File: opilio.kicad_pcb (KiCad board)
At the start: 4 copper layers, 75 x 46 mm, 113 parts, among them J1 SATA_Power_Connector, J2 USB_C_Receptacle_USB2.0, J3 Conn_01x04_Male, J6 Conn_01x06_Male, Q1 CJ3134KW, Q2 AO3401A, Q3 CJ3134KW, Q4 AO3401A, SW1 Reset, SW2 Boot, U1 EUP3458, U2 STM32F103C8T6, U3 USBLC6-2SC6, Y1 TAXM8M4RFDCET2T, Y2 YST310S 32.768KHz

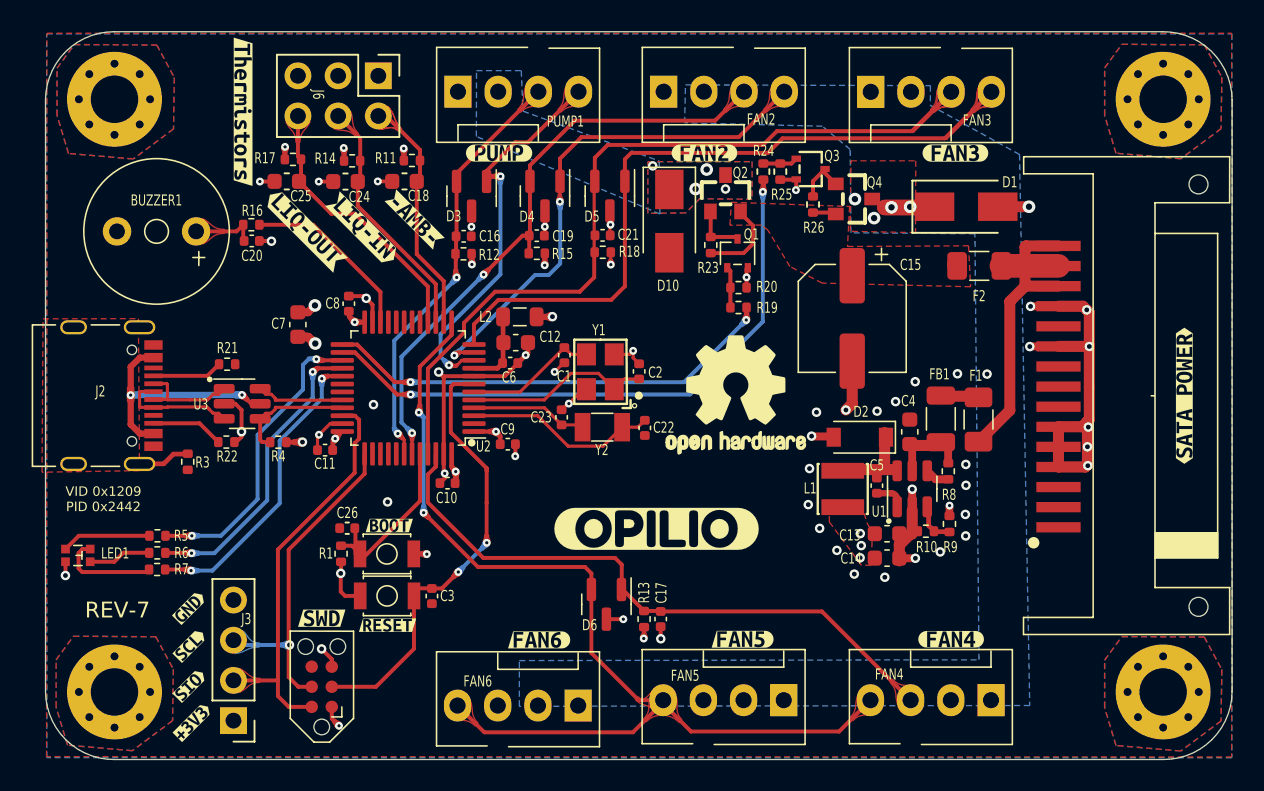
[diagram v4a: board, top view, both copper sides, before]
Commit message: split schema, re-route, horizontal fan connectors
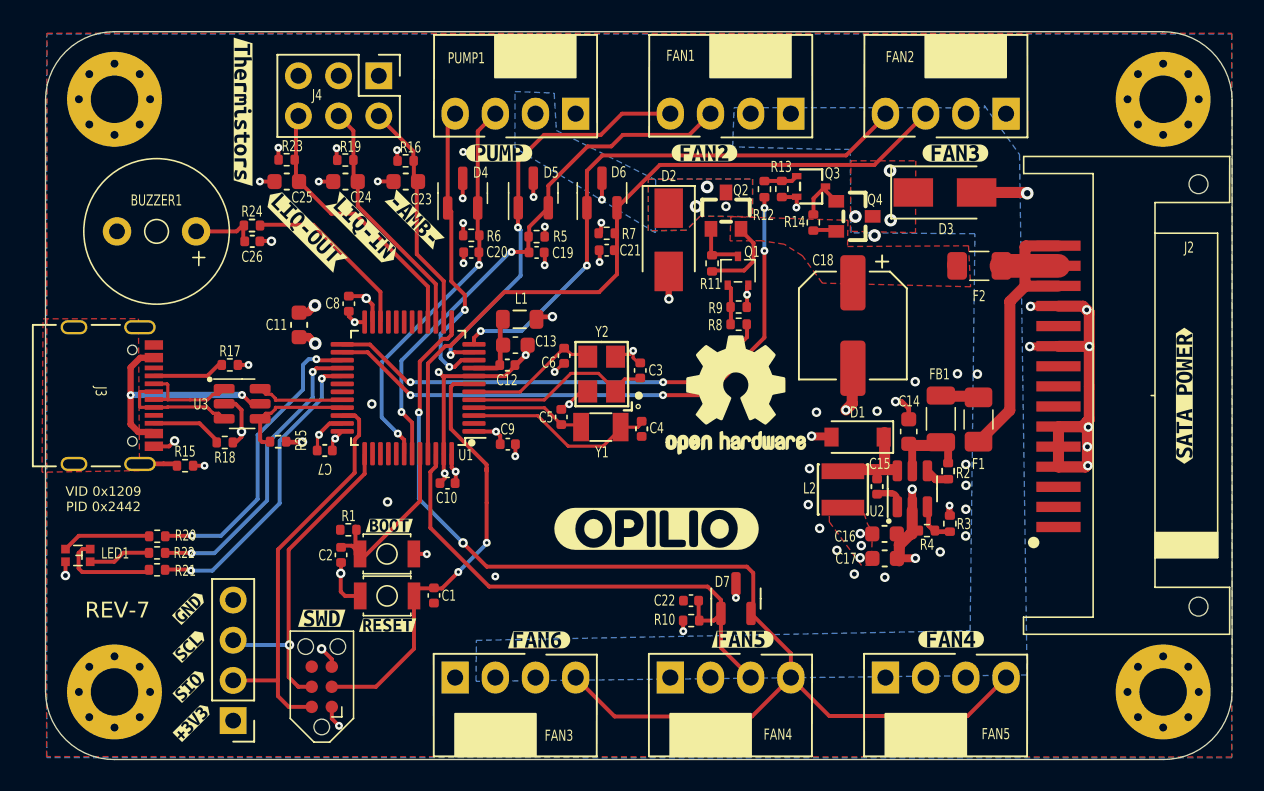
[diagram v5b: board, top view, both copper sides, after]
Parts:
- removed D10: B230A, Diode_SMD:D_SMA
- removed FAN6: Fan_4pin, Custom:FanPinHeader_1x04_P2.54mm_Vertical_no_hole
- removed J6: Conn_01x06_Male, Connector_PinHeader_2.54mm:PinHeader_2x03_P2.54mm_Vertical
- removed R26: 10K, Resistor_SMD:R_0402_1005Metric
- added D7: SP0502BAHT, Package_TO_SOT_SMD:SOT-23, F.Cu at (148.7, 132.8)
- added FAN1: Fan_4pin, Custom:FanPinHeader_1x04_P2.54mm_Horizontal_no_hole, F.Cu at (148.4, 102.2)
- added J4: Conn_01x06_Male, Connector_PinHeader_2.54mm:PinHeader_2x03_P2.54mm_Vertical, F.Cu at (126.1, 99.8)
- added R2: 1K5, Resistor_SMD:R_0402_1005Metric, F.Cu at (162.1, 124.8)
- C1, C2: value 18pF -> 100nF
- C11: value 100nF -> 10uF; footprint Capacitor_SMD:C_0402_1005Metric -> Capacitor_SMD:C_0603_1608Metric
- C12: value 10uF -> 10nF; footprint Capacitor_SMD:C_0603_1608Metric -> Capacitor_SMD:C_0402_1005Metric
- C15: value 220uF -> 10nF; footprint Capacitor_SMD:CP_Elec_6.3x7.7 -> Capacitor_SMD:C_0402_1005Metric
- C16, C17: value 10nF -> 10uF; footprint Capacitor_SMD:C_0402_1005Metric -> Capacitor_SMD:C_0603_1608Metric
- C18: value 10uF -> 220uF; footprint Capacitor_SMD:C_0603_1608Metric -> Capacitor_SMD:CP_Elec_6.3x7.7
- C20: value 100nF -> 10nF
- C22: value 18pF -> 10nF
- C23: value 18pF -> 10uF; footprint Capacitor_SMD:C_0402_1005Metric -> Capacitor_SMD:C_0603_1608Metric
- C3: value 100nF -> 18pF
- C4: value 10uF -> 18pF; footprint Capacitor_SMD:C_0603_1608Metric -> Capacitor_SMD:C_0402_1005Metric
- C5, C6: value 10nF -> 18pF
- C7: value 10uF -> 100nF; footprint Capacitor_SMD:C_0603_1608Metric -> Capacitor_SMD:C_0402_1005Metric
- D1: value B230A -> B5819W; footprint Diode_SMD:D_SMA -> Diode_SMD:D_SOD-123
- D2: value B5819W -> B230A; footprint Diode_SMD:D_SOD-123 -> Diode_SMD:D_SMA
- D3: value SP0502BAHT -> B230A; footprint Package_TO_SOT_SMD:SOT-23 -> Diode_SMD:D_SMA
- FAN2, FAN3, FAN4, FAN5, PUMP1: footprint Custom:FanPinHeader_1x04_P2.54mm_Vertical_no_hole -> Custom:FanPinHeader_1x04_P2.54mm_Horizontal_no_hole
- J1: value SATA_Power_Connector -> Conn_01x04_Male; footprint Custom:Sata_Power_Connector_SMD -> Connector_PinHeader_2.54mm:PinHeader_1x04_P2.54mm_Vertical
- J2: value USB_C_Receptacle_USB2.0 -> SATA_Power_Connector; footprint Custom:USB_C_Receptacle_Palconn_UTC16-G_Streached_pads -> Custom:Sata_Power_Connector_SMD
- J3: value Conn_01x04_Male -> USB_C_Receptacle_USB2.0; footprint Connector_PinHeader_2.54mm:PinHeader_1x04_P2.54mm_Vertical -> Custom:USB_C_Receptacle_Palconn_UTC16-G_Streached_pads
- L1: value SMNR3010-4R7MT -> 39nH; footprint easyeda2kicad:IND-SMD_L3.0-W3.0_SMNR3010 -> Inductor_SMD:L_0805_2012Metric
- L2: value 39nH -> SMNR3010-4R7MT; footprint Inductor_SMD:L_0805_2012Metric -> easyeda2kicad:IND-SMD_L3.0-W3.0_SMNR3010
- R10: value 24K -> 1K5
- R12, R8: value 1K5 -> 0R
- R13: value 1K5 -> 10K
- R15: value 1K5 -> 75K
- R16: value 100R -> 10K
- R17: value 10K -> 5K11
- R18: value 1K5 -> 5K11
- R19: value 0R -> 10K
- R20, R25: value 10K -> 1K5
- R21, R22: value 5K11 -> 1K5
- R24: value 0R -> 100R
- R4: value 1K5 -> 24K
- R9: value 75K -> 10K
- U1: value EUP3458 -> STM32F103C8T6; footprint Package_TO_SOT_SMD:SOT-23-6 -> Package_QFP:LQFP-48_7x7mm_P0.5mm
- U2: value STM32F103C8T6 -> EUP3458; footprint Package_QFP:LQFP-48_7x7mm_P0.5mm -> Package_TO_SOT_SMD:SOT-23-6
- Y1: value TAXM8M4RFDCET2T -> YST310S 32.768KHz; footprint easyeda2kicad:OSC-SMD_4P-L3.2-W2.5-BL -> Crystal:Crystal_SMD_3215-2Pin_3.2x1.5mm
- Y2: value YST310S 32.768KHz -> TAXM8M4RFDCET2T; footprint Crystal:Crystal_SMD_3215-2Pin_3.2x1.5mm -> easyeda2kicad:OSC-SMD_4P-L3.2-W2.5-BL
- moved J2 58.6 mm to (167.7, 120.0), turned to 90 degrees
- moved J1 54.8 mm to (116.9, 140.6), turned to 180 degrees
- moved R3 48.3 mm to (162.2, 128.1), turned to -90 degrees
- moved FAN3 43.5 mm to (134.8, 137.8)
- moved R4 41.4 mm to (160.8, 128.6)
- moved R20 40.0 mm to (112.1, 128.9)
- moved R25 36.0 mm to (119.8, 122.9), turned to 180 degrees
- moved R7 35.5 mm to (140.6, 109.8), turned to 0 degrees
- moved C16 32.6 mm to (158.1, 128.8), turned to 0 degrees
- moved U2 32.5 mm to (159.9, 125.9), turned to 90 degrees
- moved R24 32.5 mm to (118.1, 109.3), turned to 180 degrees
- moved U1 32.5 mm to (128.0, 119.5), turned to 180 degrees
- moved R5 30.5 mm to (136.1, 110.0)
- moved D3 29.9 mm to (161.9, 107.2), turned to 0 degrees
- moved C18 29.8 mm to (156.1, 115.6), turned to -90 degrees
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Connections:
- C1 pad 1: OSCOUT -> NRST
- C13 pad 1: +3.3V -> VDDA
- C14 pad 1: +3.3V -> Net-(C14-Pad1)
- C15 pad 1: +12VF(F) -> Net-(C15-Pad1)
- C15 pad 2: GND -> Net-(C15-Pad2)
- C16 pad 1: GND -> +3.3V
- C16 pad 2: PWM_READ1 -> GND
- C17 pad 1: GND -> +3.3V
- C17 pad 2: PWM_READ4 -> GND
- C18 pad 1: AMBIENT_T -> +12VF(F)
- C2 pad 1: GND -> BOOT0
- C2 pad 2: OSCIN -> GND
- C20 pad 1: Net-(BUZZER1-Pad1) -> GND
- C20 pad 2: GND -> PWM_READ1
- C22 pad 1: CIN -> GND
- C22 pad 2: GND -> PWM_READ4
- C23 pad 1: COUT -> AMBIENT_T
- C26 pad 1: BOOT0 -> Net-(BUZZER1-Pad1)
- C3 pad 1: NRST -> GND
- C3 pad 2: GND -> OSCIN
- C4 pad 1: Net-(C4-Pad1) -> CIN
- C5 pad 1: Net-(C5-Pad1) -> COUT
- C5 pad 2: Net-(C5-Pad2) -> GND
- C6 pad 1: VDDA -> OSCOUT
- D1 pad 1: 12vC -> Net-(C15-Pad1)
- D2 pad 1: Net-(C5-Pad1) -> 12vP
- D3 pad 1: PWM_OUT1 -> 12vC
- D3 pad 2: PWM_READ1 -> GND
- D4 pad 1: PWM_OUT2 -> PWM_OUT1
- D4 pad 2: PWM_READ2 -> PWM_READ1
- D5 pad 1: PWM_OUT3 -> PWM_OUT2
- D5 pad 2: PWM_READ3 -> PWM_READ2
- D6 pad 1: PWM_READ4 -> PWM_OUT3
- D6 pad 2: PWM_OUT4 -> PWM_READ3
- FAN2 pad 3: PWM_READ2 -> PWM_READ3
- FAN2 pad 4: PWM_OUT2 -> PWM_OUT3
- FAN3 pad 3: PWM_READ3 -> unconnected-(FAN3-Pad3)
- FAN3 pad 4: PWM_OUT3 -> PWM_OUT4
- FB1 pad 1: Net-(C4-Pad1) -> Net-(C14-Pad1)
- J1 pad 1: unconnected-(J1-Pad1) -> +3.3V
- J1 pad 2: unconnected-(J1-Pad2) -> SWIO
- J1 pad 3: unconnected-(J1-Pad3) -> SWCLK
- L1 pad 1: Net-(C5-Pad1) -> +3.3V
- L1 pad 2: +3.3V -> VDDA
- L2 pad 1: +3.3V -> Net-(C15-Pad1)
- L2 pad 2: VDDA -> +3.3V
- R10 pad 1: BUCK_FB -> +3.3V
- R10 pad 2: GND -> PWM_READ4
- R11 pad 1: AMBIENT_T -> +12VF(F)
- R11 pad 2: +3.3V -> Net-(Q1-Pad3)
- R12 pad 1: +3.3V -> FAN_EN
- R12 pad 2: PWM_READ1 -> Net-(Q3-Pad1)
- R13 pad 1: +3.3V -> GND
- R13 pad 2: PWM_READ4 -> Net-(Q3-Pad1)
- R14 pad 1: WATER_IN_T -> +12VF(F)
- R14 pad 2: +3.3V -> Net-(Q3-Pad3)
- R15 pad 1: +3.3V -> GND
- R15 pad 2: PWM_READ2 -> Net-(J3-PadS1)
- R16 pad 1: BUZZER -> AMBIENT_T
- R16 pad 2: Net-(BUZZER1-Pad1) -> +3.3V
- R17 pad 1: WATER_OUT_T -> GND
- R17 pad 2: +3.3V -> Net-(J3-PadA5)
- R18 pad 1: +3.3V -> GND
- R18 pad 2: PWM_READ3 -> Net-(J3-PadB5)
- R19 pad 1: PUMP_EN -> WATER_IN_T
- R19 pad 2: Net-(Q1-Pad1) -> +3.3V
- R20 pad 1: GND -> RED_LED
- R20 pad 2: Net-(Q1-Pad1) -> Net-(LED1-Pad1)
- R21 pad 1: GND -> GREEN_LED
- R21 pad 2: Net-(J2-PadA5) -> Net-(LED1-Pad2)
- R22 pad 1: GND -> BLUE_LED
- R22 pad 2: Net-(J2-PadB5) -> Net-(LED1-Pad4)
- R23 pad 1: +12VF(F) -> WATER_OUT_T
- R23 pad 2: Net-(Q1-Pad3) -> +3.3V
- R24 pad 1: FAN_EN -> BUZZER
- R24 pad 2: Net-(Q3-Pad1) -> Net-(BUZZER1-Pad1)
- R25 pad 1: GND -> +3.3V
- R25 pad 2: Net-(Q3-Pad1) -> USB_D+
- R3 pad 1: GND -> +3.3V
- R3 pad 2: Net-(J2-PadS1) -> BUCK_FB
- R4 pad 1: +3.3V -> BUCK_FB
- R4 pad 2: USB_D+ -> GND
- R5 pad 1: RED_LED -> +3.3V
- R5 pad 2: Net-(LED1-Pad1) -> PWM_READ2
- R6 pad 1: BLUE_LED -> +3.3V
- R6 pad 2: Net-(LED1-Pad4) -> PWM_READ1
- R7 pad 1: GREEN_LED -> +3.3V
- R7 pad 2: Net-(LED1-Pad2) -> PWM_READ3
- R8 pad 1: Net-(C4-Pad1) -> PUMP_EN
- R8 pad 2: Net-(R8-Pad2) -> Net-(Q1-Pad1)
- R9 pad 1: +3.3V -> GND
- R9 pad 2: BUCK_FB -> Net-(Q1-Pad1)
- U1 pad 1: Net-(C5-Pad2) -> +3.3V
- U1 pad 2: GND -> unconnected-(U1-Pad2)
- U1 pad 3: BUCK_FB -> CIN
- U1 pad 4: Net-(R8-Pad2) -> COUT
- U1 pad 5: Net-(C4-Pad1) -> OSCIN
- U1 pad 6: Net-(C5-Pad1) -> OSCOUT
- U2 pad 1: +3.3V -> Net-(C15-Pad2)
- U2 pad 2: unconnected-(U2-Pad2) -> GND
- U2 pad 3: CIN -> BUCK_FB
- U2 pad 4: COUT -> Net-(R2-Pad2)
- U2 pad 5: OSCIN -> Net-(C14-Pad1)
- U2 pad 6: OSCOUT -> Net-(C15-Pad1)
- Y1 pad 1: OSCIN -> CIN
- Y1 pad 2: GND -> COUT
- Y2 pad 1: CIN -> OSCIN
- Y2 pad 2: COUT -> GND
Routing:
- net PWM_OUT3: track 59.3 -> 35.7 mm, vias 0 -> 2
- net PWM_READ3: track 62.6 -> 46.2 mm
- net PWM_OUT4: track 65.2 -> 74.0 mm
- net GND: track 85.1 -> 93.6 mm, vias 56 -> 64
- net PWM_READ2: track 42.0 -> 33.8 mm
- net PWM_OUT1: track 25.9 -> 18.6 mm
- net Net-(C5-Pad1): track 6.75 -> 0.00 mm
- net Net-(C15-Pad1): track 0.00 -> 6.75 mm
- net PWM_OUT2: track 33.0 -> 26.6 mm
- net PWM_READ4: track 39.8 -> 33.5 mm
- net Net-(C4-Pad1): track 5.07 -> 0.00 mm
- net Net-(C14-Pad1): track 0.00 -> 5.07 mm
- net Net-(J3-PadB5): track 0.00 -> 4.59 mm
- net Net-(J2-PadB5): track 4.59 -> 0.00 mm
- net Net-(J3-PadA5): track 0.00 -> 4.45 mm
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- added copper zone on F.Cu, net Net-(J3-PadS1)
- removed copper zone on F.Cu, net Net-(J2-PadS1)

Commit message: rev-7 ready
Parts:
- removed kibuzzard-63630176: G***, kibuzzard-63630176
- removed kibuzzard-6364685F: G***, kibuzzard-6364685F
- removed kibuzzard-6368E60E: G***, kibuzzard-6368E60E
- removed kibuzzard-6368E619: G***, kibuzzard-6368E619
- removed kibuzzard-6368E624: G***, kibuzzard-6368E624
- added REF**: Fiducial_0.5mm_Mask1mm, Fiducial:Fiducial_0.5mm_Mask1mm, F.Cu at (169.6, 102.0)
- added REF**: Fiducial_0.5mm_Mask1mm, Fiducial:Fiducial_0.5mm_Mask1mm, F.Cu at (169.6, 138.0)
- added REF**: Fiducial_0.5mm_Mask1mm, Fiducial:Fiducial_0.5mm_Mask1mm, F.Cu at (142.6, 120.0)
- added kibuzzard-636BA6E5: G***, kibuzzard-636BA6E5, F.Cu at (119.9, 141.6)
- added kibuzzard-636BA708: G***, kibuzzard-636BA708, F.Cu at (129.6, 128.5)
- added kibuzzard-636BA711: G***, kibuzzard-636BA711, F.Cu at (129.9, 133.0)
- added kibuzzard-636C2D8A: G***, kibuzzard-636C2D8A, F.Cu at (148.2, 135.4)
- added kibuzzard-636C2D92: G***, kibuzzard-636C2D92, F.Cu at (162.3, 135.4)
- L1: footprint Inductor_SMD:L_0805_2012Metric -> Inductor_SMD:L_0603_1608Metric
- SW1: value Reset -> TS-1077S-01726; footprint easyeda2kicad:SW-SMD_L3.0-W2.5-P3.40-LS4.0-L -> easyeda2kicad:KEY-SMD_4P-L3.1-W3.1-P2.00_TS-1077S-01726
- SW2: value Boot -> TS-1077S-01726; footprint easyeda2kicad:SW-SMD_L3.0-W2.5-P3.40-LS4.0-L -> easyeda2kicad:KEY-SMD_4P-L3.1-W3.1-P2.00_TS-1077S-01726
- moved C1 6.28 mm to (123.4, 133.0), turned to 90 degrees
- moved C2 5.58 mm to (127.2, 125.7), turned to 180 degrees
- moved kibuzzard-6363013C 1.80 mm to (148.5, 104.6)
- moved kibuzzard-63646865 1.56 mm to (134.7, 135.4)
- moved SW2 1.55 mm to (126.3, 128.5)
- moved kibuzzard-636300D1 1.46 mm to (135.2, 104.6)
- moved R1 0.96 mm to (123.3, 128.6), turned to -90 degrees
- moved SW1 0.44 mm to (126.3, 132.9)
- moved L1 0.29 mm to (134.8, 115.3)
- moved R24 0.19 mm to (118.2, 109.1)
- moved C26 0.19 mm to (118.2, 110.1)
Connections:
- SW1 pad 1: GND -> NRST
- SW2 pad 1: BOOT0 -> +3.3V
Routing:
- net NRST: track 29.7 -> 34.8 mm
- net GND: track 93.6 -> 98.1 mm, vias 64 -> 65
- net +3.3V: track 18.7 -> 22.1 mm
- net BOOT0: track 11.6 -> 10.1 mm
- net 12vP: vias 3 -> 4
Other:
- board text added: "*"
- board text added: "0.25A"
- board text added: "2A"

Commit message: fix led polarity
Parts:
- removed REF** (x3): Fiducial_0.5mm_Mask1mm, Fiducial:Fiducial_0.5mm_Mask1mm
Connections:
- LED1 pad 3: GND -> +3.3V
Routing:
- net GND: track 98.1 -> 97.2 mm, vias 65 -> 64
- net +3.3V: track 22.1 -> 23.0 mm, vias 20 -> 21
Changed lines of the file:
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@@
     )
   )
-  (footprint "Fiducial:Fiducial_0.5mm_Mask1mm" (layer "F.Cu")
-    (at 169.58 102.02)
-    (descr "Circular Fiducial, 0.5mm bare copper, 1mm soldermask opening (Level C)")
-    (tags "fiducial")
-    (attr smd)
-    (fp_text reference "REF**" (at 2.78 0.91) (layer "F.SilkS") hide
-      (effects (font (size 1 1) (thickness 0.15)))
-    )
-    (fp_text value "Fiducial_0.5mm_Mask1mm" (at 0 1.5) (layer "F.Fab")
-      (effects (font (size 1 1) (thickness 0.15)))
-    )
-    (fp_text user "${REFERENCE}" (at 0 0) (layer "F.Fab")
-      (effects (font (size 0.2 0.2) (thickness 0.04)))
-    )
-    (fp_circle (center 0 0) (end 0.6 0.02) (layer "F.CrtYd") (width 0.05) (fill none))
-    (fp_circle (center 0 0) (end 0.5 0) (layer "F.Fab") (width 0.1) (fill none))
-    (pad "" smd circle (at 0 0) (size 0.5 0.5) (layers "F.Cu" "F.Mask")
-      (solder_mask_margin 0.25) (clearance 0.25))
-  )
   (footprint "Resistor_SMD:R_0402_1005Metric" locked (layer "F.Cu")
     (at 160.79 128.55 180)
@@
       (net 40 "Net-(LED1-Pad2)") (pinfunction "2") (pintype "unspecified"))
     (pad "3" smd rect locked (at 0.78 -0.4) (size 0.55 0.55) (layers "F.Cu" "F.Paste" "F.Mask")
-      (net 3 "GND") (pinfunction "3") (pintype "unspecified"))
+      (net 29 "+3.3V") (pinfunction "3") (pintype "unspecified"))
     (pad "4" smd rect locked (at -0.78 -0.4) (size 0.55 0.55) (layers "F.Cu" "F.Paste" "F.Mask")
       (net 41 "Net-(LED1-Pad4)") (pinfunction "4") (pintype "unspecified"))
@@
     )
   )
-  (footprint "Fiducial:Fiducial_0.5mm_Mask1mm" (layer "F.Cu")
-    (at 169.58 138.02)
-    (descr "Circular Fiducial, 0.5mm bare copper, 1mm soldermask opening (Level C)")
-    (tags "fiducial")
-    (attr smd)
-    (fp_text reference "REF**" (at 2.78 0.91) (layer "F.SilkS") hide
-      (effects (font (size 1 1) (thickness 0.15)))
-    )
-    (fp_text value "Fiducial_0.5mm_Mask1mm" (at 0 1.5) (layer "F.Fab")
-      (effects (font (size 1 1) (thickness 0.15)))
-    )
-    (fp_text user "${REFERENCE}" (at 0 0) (layer "F.Fab")
-      (effects (font (size 0.2 0.2) (thickness 0.04)))
-    )
-    (fp_circle (center 0 0) (end 0.6 0.02) (layer "F.CrtYd") (width 0.05) (fill none))
-    (fp_circle (center 0 0) (end 0.5 0) (layer "F.Fab") (width 0.1) (fill none))
-    (pad "" smd circle (at 0 0) (size 0.5 0.5) (layers "F.Cu" "F.Mask")
-      (solder_mask_margin 0.25) (clearance 0.25))
-  )
   (footprint "kibuzzard-63646865" (layer "F.Cu")
     (at 134.72 135.4)
@@
       ) (layer "F.SilkS") (width 0) (fill solid))
   )
-  (footprint "Fiducial:Fiducial_0.5mm_Mask1mm" (layer "F.Cu")
-    (at 142.58 120.02)
-    (descr "Circular Fiducial, 0.5mm bare copper, 1mm soldermask opening (Level C)")
-    (tags "fiducial")
-    (attr smd)
-    (fp_text reference "REF**" (at 2.78 0.91) (layer "F.SilkS") hide
-      (effects (font (size 1 1) (thickness 0.15)))
-    )
-    (fp_text value "Fiducial_0.5mm_Mask1mm" (at 0 1.5) (layer "F.Fab")
-      (effects (font (size 1 1) (thickness 0.15)))
-    )
-    (fp_text user "${REFERENCE}" (at 0 0) (layer "F.Fab")
-      (effects (font (size 0.2 0.2) (thickness 0.04)))
-    )
-    (fp_circle (center 0 0) (end 0.6 0.02) (layer "F.CrtYd") (width 0.05) (fill none))
-    (fp_circle (center 0 0) (end 0.5 0) (layer "F.Fab") (width 0.1) (fill none))
-    (pad "" smd circle (at 0 0) (size 0.5 0.5) (layers "F.Cu" "F.Mask")
-      (solder_mask_margin 0.25) (clearance 0.25))
-  )
   (footprint "Resistor_SMD:R_0402_1005Metric" (layer "F.Cu")
     (at 147.21 111.66 90)
@@
   (segment (start 170.81 124.53) (end 170.935 124.405) (width 0.7) (layer "F.Cu") (net 3))
   (segment (start 136.64 110.95) (end 136.64 111.73) (width 0.25) (layer "F.Cu") (net 3))
-  (segment (start 106.34375 130.52) (end 106.34375 131.38625) (width 0.25) (layer "F.Cu") (net 3))
   (segment (start 119.365 110.055) (end 119.38 110.07) (width 0.25) (layer "F.Cu") (net 3))
   (segment (start 170.59 121.99) (end 169.105 121.99) (width 0.7) (layer "F.Cu") (net 3))
   (segment (start 117.470001 120.924999) (end 117.470001 122.299999) (width 0.25) (layer "F.Cu") (net 3))
   (segment (start 169.105 124.53) (end 170.81 124.53) (width 0.7) (layer "F.Cu") (net 3))
-  (segment (start 106.34375 131.38625) (end 106.34 131.39) (width 0.25) (layer "F.Cu") (net 3))
   (segment (start 154.874999 122.6) (end 153.52 122.6) (width 0.5) (layer "F.Cu") (net 3))
   (segment (start 121.030002 114.755002) (end 121.675 114.755) (width 0.5) (layer "F.Cu") (net 3))
@@
   (via (at 163.98 118.66) (size 0.6) (drill 0.3) (layers "F.Cu" "B.Cu") (free) (net 3))
   (via (at 162.72 118.64) (size 0.6) (drill 0.3) (layers "F.Cu" "B.Cu") (free) (net 3))
-  (via (at 106.34 131.39) (size 0.6) (drill 0.3) (layers "F.Cu" "B.Cu") (net 3))
   (via (at 155.1 129.8) (size 0.6) (drill 0.3) (layers "F.Cu" "B.Cu") (free) (net 3))
   (via (at 131.5 111.65) (size 0.5) (drill 0.2) (layers "F.Cu" "B.Cu") (net 3))
@@
   (segment (start 123.48 105.234999) (end 123.48 104.445001) (width 0.25) (layer "F.Cu") (net 29))
   (segment (start 124.25 114.69) (end 124.25 115.005) (width 0.25) (layer "F.Cu") (net 29))
+  (segment (start 106.34375 130.52) (end 106.34375 131.38625) (width 0.25) (layer "F.Cu") (net 29))
   (segment (start 136.64 109.34) (end 136.64 109.88) (width 0.2) (layer "F.Cu") (net 29))
+  (segment (start 106.34375 131.38625) (end 106.34 131.39) (width 0.25) (layer "F.Cu") (net 29))
   (segment (start 124.6225 115.3775) (end 125.25 115.3775) (width 0.25) (layer "F.Cu") (net 29))
   (segment (start 131.007096 125.312904) (end 131.007096 124.821743) (width 0.2) (layer "F.Cu") (net 29))
@@
   (via (at 123.38875 122.73875) (size 0.5) (drill 0.2) (layers "F.Cu" "B.Cu") (net 29))
   (via (at 131.007096 124.821743) (size 0.5) (drill 0.2) (layers "F.Cu" "B.Cu") (net 29))
+  (via (at 106.34 131.39) (size 0.6) (drill 0.3) (layers "F.Cu" "B.Cu") (net 29))
   (via (at 119.8 104.35) (size 0.5) (drill 0.2) (layers "F.Cu" "B.Cu") (net 29))
   (segment (start 121.998746 109.22) (end 126.25 113.471254) (width 0.25) (layer "F.Cu") (net 30))

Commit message: cleanup
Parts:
- removed FAN1: Fan_4pin, Custom:FanPinHeader_1x04_P2.54mm_Horizontal_no_hole
- removed kibuzzard-6362FF8D: G***, kibuzzard-6362FF8D
- removed kibuzzard-6362FF97: G***, kibuzzard-6362FF97
- removed kibuzzard-6363003C: G***, kibuzzard-6363003C
- removed kibuzzard-636300D1: G***, kibuzzard-636300D1
- removed kibuzzard-6363013C: G***, kibuzzard-6363013C
- removed kibuzzard-6363014F: G***, kibuzzard-6363014F
- removed kibuzzard-636302D8: G***, kibuzzard-636302D8
- removed kibuzzard-63646865: G***, kibuzzard-63646865
- removed kibuzzard-636468A0: G***, kibuzzard-636468A0
- removed kibuzzard-6368E566: G***, kibuzzard-6368E566
- removed kibuzzard-6368E571: G***, kibuzzard-6368E571
- removed kibuzzard-6368E578: G***, kibuzzard-6368E578
- removed kibuzzard-6368E57E: G***, kibuzzard-6368E57E
- removed kibuzzard-6368E8DC: G***, kibuzzard-6368E8DC
- removed kibuzzard-636BA708: G***, kibuzzard-636BA708
- removed kibuzzard-636BA711: G***, kibuzzard-636BA711
- removed kibuzzard-636C2D8A: G***, kibuzzard-636C2D8A
- removed kibuzzard-636C2D92: G***, kibuzzard-636C2D92
- added FAN6: Fan_4pin, Custom:FanPinHeader_1x04_P2.54mm_Horizontal_no_hole, F.Cu at (134.8, 137.8)
- added kibuzzard-63853BC6: G***, kibuzzard-63853BC6, F.Cu at (117.6, 102.1)
- added kibuzzard-63853BFA: G***, kibuzzard-63853BFA, F.Cu at (129.9, 133.0)
- added kibuzzard-63853C04: G***, kibuzzard-63853C04, F.Cu at (129.6, 128.5)
- added kibuzzard-63853C0D: G***, kibuzzard-63853C0D, F.Cu at (134.7, 135.4)
- added kibuzzard-63853C6A: G***, kibuzzard-63853C6A, F.Cu at (162.6, 104.7)
- added kibuzzard-63853C76: G***, kibuzzard-63853C76, F.Cu at (148.5, 104.6)
- added kibuzzard-63853C81: G***, kibuzzard-63853C81, F.Cu at (135.2, 104.6)
- added kibuzzard-63853CA9: G***, kibuzzard-63853CA9, F.Cu at (143.7, 128.4)
- added kibuzzard-63853CCB: G***, kibuzzard-63853CCB, F.Cu at (177.1, 120.0)
- added kibuzzard-63853D5C: G***, kibuzzard-63853D5C, F.Cu at (114.2, 133.4)
- added kibuzzard-63853D64: G***, kibuzzard-63853D64, F.Cu at (114.2, 135.8)
- added kibuzzard-63853D6B: G***, kibuzzard-63853D6B, F.Cu at (114.2, 138.3)
- added kibuzzard-63853D72: G***, kibuzzard-63853D72, F.Cu at (114.4, 140.7)
- added kibuzzard-638555C7: G***, kibuzzard-638555C7, F.Cu at (121.5, 109.6)
- added kibuzzard-638555D0: G***, kibuzzard-638555D0, F.Cu at (125.1, 109.6)
- added kibuzzard-638555D8: G***, kibuzzard-638555D8, F.Cu at (128.3, 109.1)
- added kibuzzard-638559F0: G***, kibuzzard-638559F0, F.Cu at (148.2, 135.4)
- added kibuzzard-638559F7: G***, kibuzzard-638559F7, F.Cu at (162.3, 135.4)
- moved FAN3 44.8 mm to (162.0, 102.2), turned to 180 degrees
- moved FAN2 13.6 mm to (148.4, 102.2)
- moved FAN4 13.6 mm to (162.0, 137.8)
- moved FAN5 13.6 mm to (148.4, 137.8)
- moved R17 2.90 mm to (113.9, 118.8)
- moved R18 2.66 mm to (113.9, 122.1)
- moved C3 0.12 mm to (142.6, 118.3)
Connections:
- FAN2 pad 3: PWM_READ3 -> PWM_READ2
- FAN2 pad 4: PWM_OUT3 -> PWM_OUT2
- FAN3 pad 3: unconnected-(FAN3-Pad3) -> PWM_READ3
- FAN3 pad 4: PWM_OUT4 -> PWM_OUT3
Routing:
- net PWM_READ4: track 33.5 -> 46.6 mm
- net PWM_OUT4: track 74.0 -> 86.5 mm
- net Net-(J3-PadB5): track 4.59 -> 1.59 mm
- net Net-(J3-PadA5): track 4.45 -> 1.49 mm
- net +5V: track 15.2 -> 17.0 mm, vias 2 -> 0
- net GND: track 97.2 -> 98.2 mm, vias 64 -> 82
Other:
- board text added: "REV-7.1"
- board text removed: "REV-7"
